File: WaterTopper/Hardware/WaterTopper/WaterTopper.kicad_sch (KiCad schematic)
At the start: 61 parts, among them J1 TYPE-C-31-M-12, J2 Barrel_Jack_Switch, J3 Conn_01x07, J4 Conn_01x04, J5 Conn_01x04, J6 Conn_01x04, J7 Conn_01x04, J8 Screw_Terminal_01x02, J9 Screw_Terminal_01x02, SW1 SW_SPST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

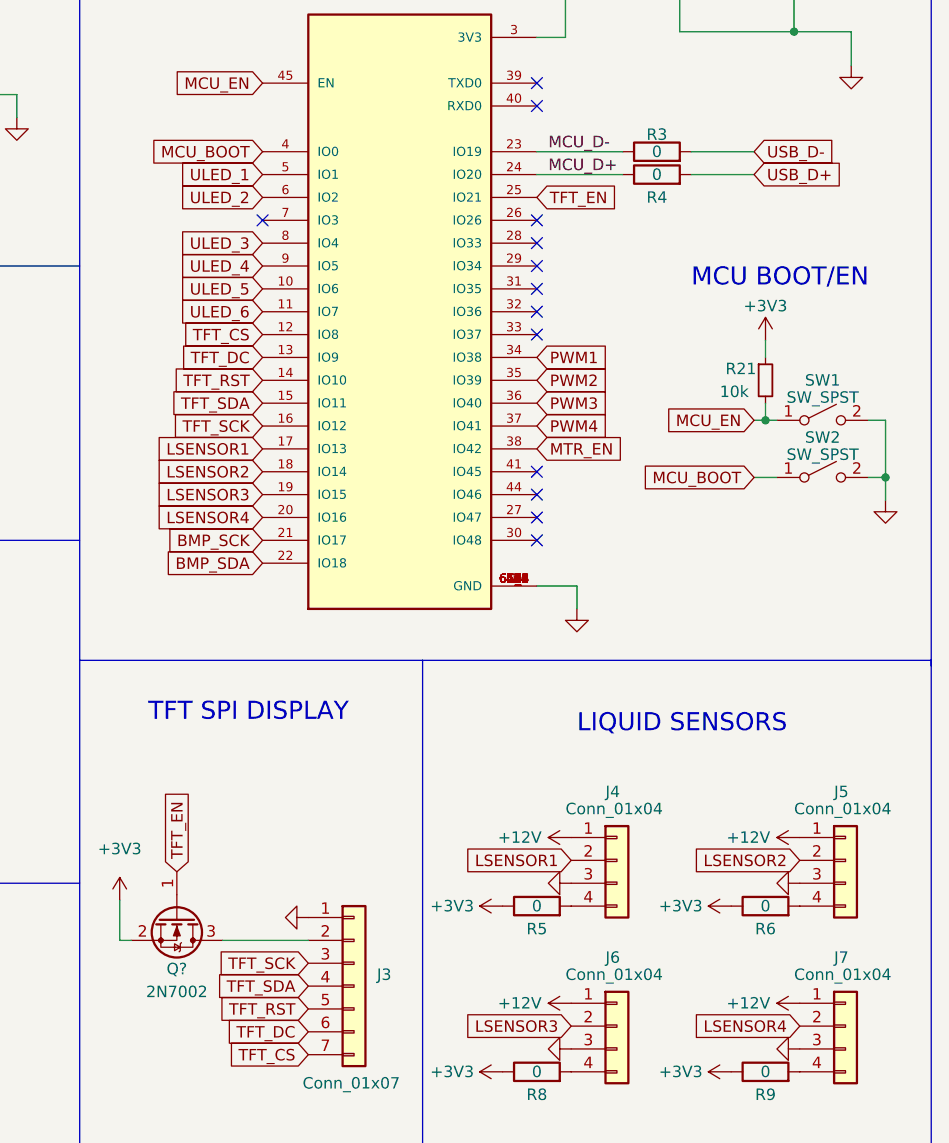
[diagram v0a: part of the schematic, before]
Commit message: Added button
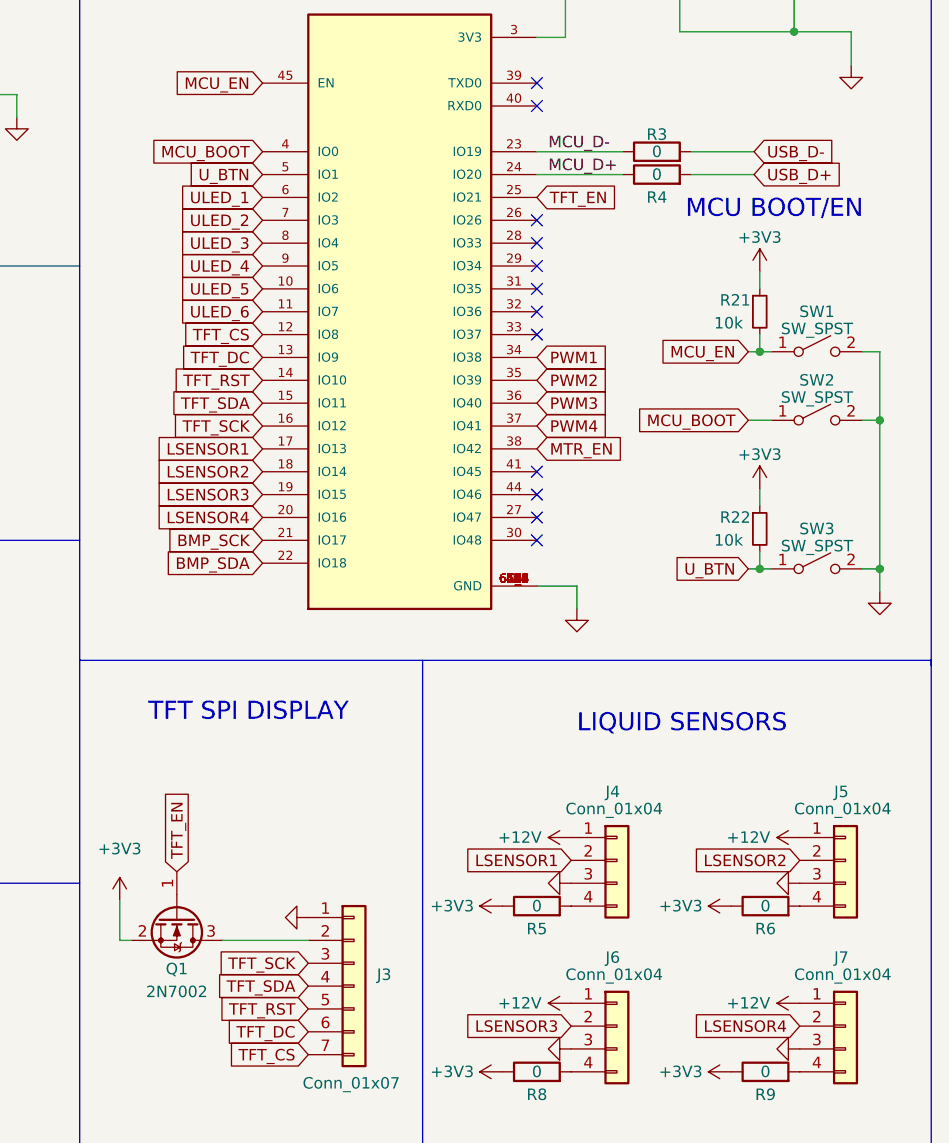
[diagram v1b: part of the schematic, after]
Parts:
- added R22: 10k, Resistor_SMD:R_0603_1608Metric, symbol Device:R_Small
- added SW3: SW_SPST, Button_Switch_THT:SW_Tactile_SPST_Angled_PTS645Vx58-2LFS, symbol Switch:SW_SPST
- gave numbers to parts that had none: 1
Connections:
- net +3V3: now also R22.1
- net GND: now also SW3.2 (B)
- net ULED_1: now also U2.6 (IO2); no longer U2.5 (IO1)
- net ULED_2: now also U2.7 (IO3); no longer U2.6 (IO2)
- new net U_BTN: R22.2, SW3.1 (A), U2.5 (IO1)
- no-connect marks 15 -> 14
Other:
- moved on the sheet: R21, SW1, SW2

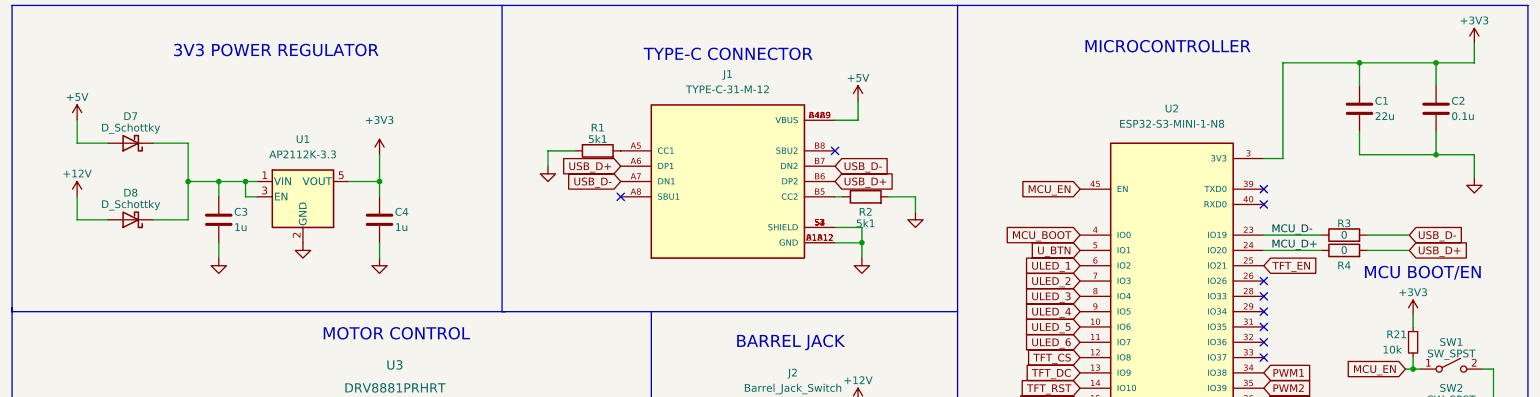
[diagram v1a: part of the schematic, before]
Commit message: Added BOM, added voltage divider
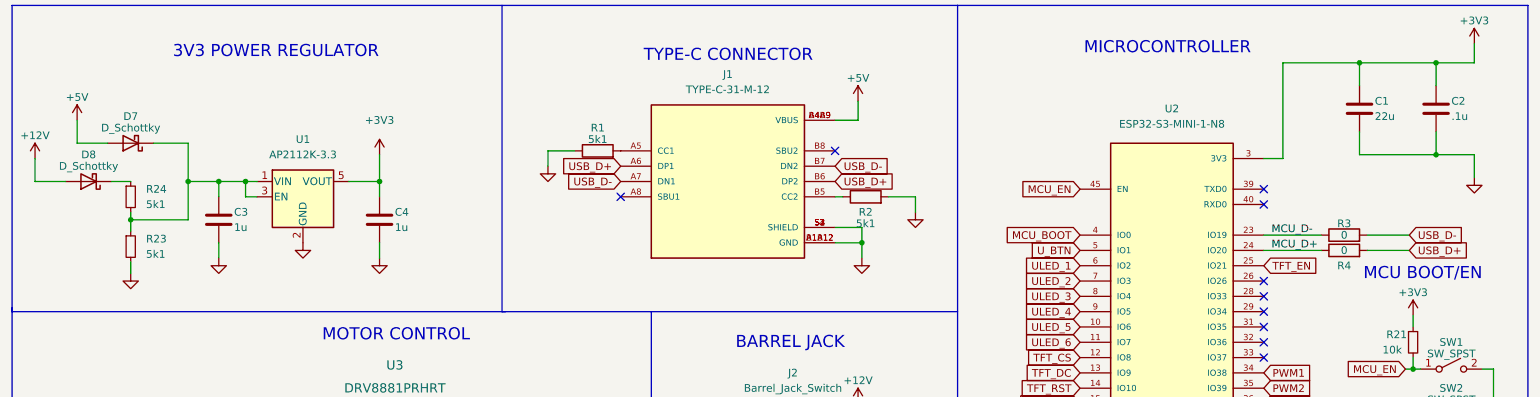
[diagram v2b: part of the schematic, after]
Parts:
- added R23, R24: 5k1, Resistor_SMD:R_0603_1608Metric, symbol Device:R_Small
- C2: value 0.1u -> .1u
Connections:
- net GND: now also R23.2
- net at C3.1, D7.1 (K), U1.1 (VIN)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: now also R23.1, R24.2; no longer D8.1 (K)
- new net: D8.1 (K), R24.1
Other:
- moved on the sheet: D8
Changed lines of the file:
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@@
   (junction (at 279.4 97.155) (diameter 0) (color 0 0 0 0)
   )
+  (junction (at 53.34 48.26) (diameter 0) (color 0 0 0 0)
+  )
   (junction (at 57.15 91.44) (diameter 0) (color 0 0 0 0)
   )
@@
     (stroke (width 0) (type default) (color 0 0 0 0))
   )
-  (wire (pts (xy 44.45 48.26) (xy 49.53 48.26))
+  (wire (pts (xy 37.465 41.91) (xy 42.545 41.91))
     (stroke (width 0) (type default) (color 0 0 0 0))
   )
@@
     (stroke (width 0) (type default) (color 0 0 0 0))
   )
+  (wire (pts (xy 53.34 48.26) (xy 53.34 50.165))
+    (stroke (width 0) (type default) (color 0 0 0 0))
+  )
   (wire (pts (xy 72.39 154.94) (xy 76.835 154.94))
     (stroke (width 0) (type default) (color 0 0 0 0))
@@
     (stroke (width 0) (type default) (color 0 0 0 0))
   )
+  (wire (pts (xy 50.165 41.91) (xy 53.34 41.91))
+    (stroke (width 0) (type default) (color 0 0 0 0))
+  )
   (wire (pts (xy 92.71 186.055) (xy 92.71 187.96))
     (stroke (width 0) (type default) (color 0 0 0 0))
@@
     (stroke (width 0) (type default) (color 0 0 0 0))
   )
+  (wire (pts (xy 53.34 55.245) (xy 53.34 57.15))
+    (stroke (width 0) (type default) (color 0 0 0 0))
+  )
   (wire (pts (xy 120.65 149.86) (xy 117.475 149.86))
     (stroke (width 0) (type default) (color 0 0 0 0))
@@
     (stroke (width 0) (type default) (color 0 0 0 0))
   )
-  (wire (pts (xy 57.15 48.26) (xy 62.865 48.26))
+  (wire (pts (xy 53.34 48.26) (xy 62.865 48.26))
     (stroke (width 0) (type default) (color 0 0 0 0))
   )
@@
     (stroke (width 0) (type default) (color 0 0 0 0))
   )
+  (wire (pts (xy 53.34 46.99) (xy 53.34 48.26))
+    (stroke (width 0) (type default) (color 0 0 0 0))
+  )
   (wire (pts (xy 72.39 157.48) (xy 72.39 154.94))
     (stroke (width 0) (type default) (color 0 0 0 0))
@@
     (stroke (width 0) (type default) (color 0 0 0 0))
   )
-  (wire (pts (xy 44.45 44.45) (xy 44.45 48.26))
+  (wire (pts (xy 37.465 38.1) (xy 37.465 41.91))
     (stroke (width 0) (type default) (color 0 0 0 0))
   )
@@
     )
   )
+  (symbol (lib_id "Device:R_Small") (at 53.34 52.705 0) (unit 1)
+    (in_bom yes) (on_board yes) (fields_autoplaced)
+    (property "Reference" "R23" (id 0) (at 55.88 51.4349 0)
+      (effects (font (size 1.27 1.27)) (justify left))
+    )
+    (property "Value" "5k1" (id 1) (at 55.88 53.9749 0)
+      (effects (font (size 1.27 1.27)) (justify left))
+    )
+    (property "Footprint" "Resistor_SMD:R_0603_1608Metric" (id 2) (at 53.34 52.705 0)
+      (effects (font (size 1.27 1.27)) hide)
+    )
+    (property "Datasheet" "~" (id 3) (at 53.34 52.705 0)
+      (effects (font (size 1.27 1.27)) hide)
+    )
+    (pin "1")
+    (pin "2")
+  )
   (symbol (lib_id "Switch:SW_SPST") (at 272.415 80.645 0) (unit 1)
     (in_bom yes) (on_board yes)
@@
     (pin "2")
   )
-  (symbol (lib_id "power:+12V") (at 44.45 44.45 0) (unit 1)
+  (symbol (lib_id "power:+12V") (at 37.465 38.1 0) (unit 1)
     (in_bom yes) (on_board yes)
-    (property "Reference" "#PWR07" (id 0) (at 44.45 48.26 0)
+    (property "Reference" "#PWR07" (id 0) (at 37.465 41.91 0)
       (effects (font (size 1.27 1.27)) hide)
     )
-    (property "Value" "+12V" (id 1) (at 44.45 40.64 0))
-    (property "Footprint" "" (id 2) (at 44.45 44.45 0)
+    (property "Value" "+12V" (id 1) (at 37.465 34.29 0))
+    (property "Footprint" "" (id 2) (at 37.465 38.1 0)
       (effects (font (size 1.27 1.27)) hide)
     )
-    (property "Datasheet" "" (id 3) (at 44.45 44.45 0)
+    (property "Datasheet" "" (id 3) (at 37.465 38.1 0)
+      (effects (font (size 1.27 1.27)) hide)
+    )
+    (pin "1")
+  )
+  (symbol (lib_id "Device:R_Small") (at 53.34 44.45 0) (unit 1)
+    (in_bom yes) (on_board yes) (fields_autoplaced)
+    (property "Reference" "R24" (id 0) (at 55.88 43.1799 0)
+      (effects (font (size 1.27 1.27)) (justify left))
+    )
+    (property "Value" "5k1" (id 1) (at 55.88 45.7199 0)
+      (effects (font (size 1.27 1.27)) (justify left))
+    )
+    (property "Footprint" "Resistor_SMD:R_0603_1608Metric" (id 2) (at 53.34 44.45 0)
+      (effects (font (size 1.27 1.27)) hide)
+    )
+    (property "Datasheet" "~" (id 3) (at 53.34 44.45 0)
+      (effects (font (size 1.27 1.27)) hide)
+    )
+    (pin "1")
+    (pin "2")
+  )
+  (symbol (lib_id "power:GND") (at 53.34 57.15 0) (unit 1)
+    (in_bom yes) (on_board yes) (fields_autoplaced)
+    (property "Reference" "#PWR017" (id 0) (at 53.34 63.5 0)
+      (effects (font (size 1.27 1.27)) hide)
+    )
+    (property "Value" "GND" (id 1) (at 53.34 62.23 0)
+      (effects (font (size 1.27 1.27)) hide)
+    )
+    (property "Footprint" "" (id 2) (at 53.34 57.15 0)
+      (effects (font (size 1.27 1.27)) hide)
+    )
+    (property "Datasheet" "" (id 3) (at 53.34 57.15 0)
       (effects (font (size 1.27 1.27)) hide)
     )
@@
     (pin "1")
   )
-  (symbol (lib_id "Device:D_Schottky") (at 53.34 48.26 180) (unit 1)
+  (symbol (lib_id "Device:D_Schottky") (at 46.355 41.91 180) (unit 1)
     (in_bom yes) (on_board yes)
-    (property "Reference" "D8" (id 0) (at 53.34 43.815 0))
-    (property "Value" "D_Schottky" (id 1) (at 53.34 45.72 0))
-    (property "Footprint" "Diode_SMD:D_SMA" (id 2) (at 53.34 48.26 0)
+    (property "Reference" "D8" (id 0) (at 46.355 37.465 0))
+    (property "Value" "D_Schottky" (id 1) (at 46.355 39.37 0))
+    (property "Footprint" "Diode_SMD:D_SMA" (id 2) (at 46.355 41.91 0)
       (effects (font (size 1.27 1.27)) hide)
     )
-    (property "Datasheet" "~" (id 3) (at 53.34 48.26 0)
+    (property "Datasheet" "~" (id 3) (at 46.355 41.91 0)
       (effects (font (size 1.27 1.27)) hide)
     )
@@
       (effects (font (size 1.27 1.27)) (justify left))
     )
-    (property "Value" "0.1u" (id 1) (at 272.415 31.115 0)
+    (property "Value" ".1u" (id 1) (at 272.415 31.115 0)
       (effects (font (size 1.27 1.27)) (justify left))
     )
@@
       (reference "#PWR016") (unit 1) (value "GND") (footprint "")
     )
+    (path "/3676a4a4-5eb8-46aa-8e32-9374a5d5329f"
+      (reference "#PWR017") (unit 1) (value "GND") (footprint "")
+    )
     (path "/80e550fc-be45-4fa3-8cfa-273205d2d6f2"
       (reference "#PWR018") (unit 1) (value "+12V") (footprint "")
@@
     )
     (path "/b0504792-045b-4e2a-b87c-567ade3ca219"
-      (reference "C2") (unit 1) (value "0.1u") (footprint "Capacitor_SMD:C_0603_1608Metric")
+      (reference "C2") (unit 1) (value ".1u") (footprint "Capacitor_SMD:C_0603_1608Metric")
     )
     (path "/8d06c145-6d1c-4c49-9640-7f572901a9e5"
@@
       (reference "R22") (unit 1) (value "10k") (footprint "Resistor_SMD:R_0603_1608Metric")
     )
+    (path "/2170c5b0-7a38-4ec4-9ff3-efd2cf79432d"
+      (reference "R23") (unit 1) (value "5k1") (footprint "Resistor_SMD:R_0603_1608Metric")
+    )
+    (path "/35dc428a-d1b2-43fc-a3e3-2f51a6c4b7f3"
+      (reference "R24") (unit 1) (value "5k1") (footprint "Resistor_SMD:R_0603_1608Metric")
+    )
     (path "/ef3fe0f0-76ed-4e85-9a29-a9bdea4e677c"

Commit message: Built small motor driver library
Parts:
- J3: footprint Connector_PinHeader_2.00mm:PinHeader_1x07_P2.00mm_Vertical -> Connector_PinHeader_2.54mm:PinHeader_1x07_P2.54mm_Vertical
- J4, J5, J6, J7: footprint Connector_JST:JST_PH_B4B-PH-K_1x04_P2.00mm_Vertical -> Connector_JST:JST_XA_B04B-XASK-1_1x04_P2.50mm_Vertical
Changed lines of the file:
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@@
       (effects (font (size 1.27 1.27)) (justify left))
     )
-    (property "Footprint" "Connector_JST:JST_PH_B4B-PH-K_1x04_P2.00mm_Vertical" (id 2) (at 275.59 129.54 0)
+    (property "Footprint" "Connector_JST:JST_XA_B04B-XASK-1_1x04_P2.50mm_Vertical" (id 2) (at 275.59 129.54 0)
       (effects (font (size 1.27 1.27)) hide)
     )
@@
       (effects (font (size 1.27 1.27)) (justify left))
     )
-    (property "Footprint" "Connector_JST:JST_PH_B4B-PH-K_1x04_P2.00mm_Vertical" (id 2) (at 250.19 129.54 0)
+    (property "Footprint" "Connector_JST:JST_XA_B04B-XASK-1_1x04_P2.50mm_Vertical" (id 2) (at 250.19 129.54 0)
       (effects (font (size 1.27 1.27)) hide)
     )
@@
       (effects (font (size 1.27 1.27)) (justify left))
     )
-    (property "Footprint" "Connector_PinHeader_2.00mm:PinHeader_1x07_P2.00mm_Vertical" (id 2) (at 220.98 143.51 0)
+    (property "Footprint" "Connector_PinHeader_2.54mm:PinHeader_1x07_P2.54mm_Vertical" (id 2) (at 220.98 143.51 0)
       (effects (font (size 1.27 1.27)) hide)
     )
@@
       (effects (font (size 1.27 1.27)) (justify left))
     )
-    (property "Footprint" "Connector_JST:JST_PH_B4B-PH-K_1x04_P2.00mm_Vertical" (id 2) (at 250.19 147.955 0)
+    (property "Footprint" "Connector_JST:JST_XA_B04B-XASK-1_1x04_P2.50mm_Vertical" (id 2) (at 250.19 147.955 0)
       (effects (font (size 1.27 1.27)) hide)
     )
@@
       (effects (font (size 1.27 1.27)) (justify left))
     )
-    (property "Footprint" "Connector_JST:JST_PH_B4B-PH-K_1x04_P2.00mm_Vertical" (id 2) (at 275.59 147.955 0)
+    (property "Footprint" "Connector_JST:JST_XA_B04B-XASK-1_1x04_P2.50mm_Vertical" (id 2) (at 275.59 147.955 0)
       (effects (font (size 1.27 1.27)) hide)
     )
@@
     )
     (path "/e2f23f31-8323-4c97-88fa-d0875c6d0034"
-      (reference "J3") (unit 1) (value "Conn_01x07") (footprint "Connector_PinHeader_2.00mm:PinHeader_1x07_P2.00mm_Vertical")
+      (reference "J3") (unit 1) (value "Conn_01x07") (footprint "Connector_PinHeader_2.54mm:PinHeader_1x07_P2.54mm_Vertical")
     )
     (path "/ae2a3736-ef68-40b1-b712-59c0bd62bbdb"
-      (reference "J4") (unit 1) (value "Conn_01x04") (footprint "Connector_JST:JST_PH_B4B-PH-K_1x04_P2.00mm_Vertical")
+      (reference "J4") (unit 1) (value "Conn_01x04") (footprint "Connector_JST:JST_XA_B04B-XASK-1_1x04_P2.50mm_Vertical")
     )
     (path "/0d8bfabd-018f-4ea5-90c0-9a8913e5d3d1"
-      (reference "J5") (unit 1) (value "Conn_01x04") (footprint "Connector_JST:JST_PH_B4B-PH-K_1x04_P2.00mm_Vertical")
+      (reference "J5") (unit 1) (value "Conn_01x04") (footprint "Connector_JST:JST_XA_B04B-XASK-1_1x04_P2.50mm_Vertical")
     )
     (path "/eb41b22b-13c2-425c-80c3-3c5c7887a444"
-      (reference "J6") (unit 1) (value "Conn_01x04") (footprint "Connector_JST:JST_PH_B4B-PH-K_1x04_P2.00mm_Vertical")
+      (reference "J6") (unit 1) (value "Conn_01x04") (footprint "Connector_JST:JST_XA_B04B-XASK-1_1x04_P2.50mm_Vertical")
     )
     (path "/fdba77c3-e1f8-4a4a-bb97-703a213c3276"
-      (reference "J7") (unit 1) (value "Conn_01x04") (footprint "Connector_JST:JST_PH_B4B-PH-K_1x04_P2.00mm_Vertical")
+      (reference "J7") (unit 1) (value "Conn_01x04") (footprint "Connector_JST:JST_XA_B04B-XASK-1_1x04_P2.50mm_Vertical")
     )
     (path "/aa44beac-9563-4b24-911f-6caba337a36b"
